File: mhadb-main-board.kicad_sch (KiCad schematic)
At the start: 113 parts, among them J1 Conn_01x04, J10 Conn_01x04_Pin, J2 Conn_01x04, J3 USB_C_Receptacle_USB2.0_14P, J4 Conn_01x02, J5 Conn_01x03, J6 Conn_01x03, J7 Conn_01x04, J8 Conn_01x04, J9 Conn_01x04_Pin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

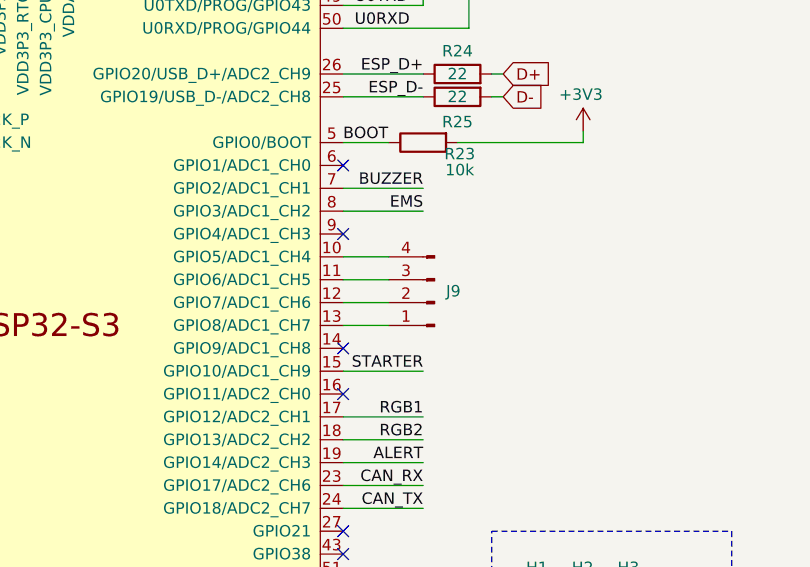
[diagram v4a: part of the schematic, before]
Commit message: pcb: changed outline to 50x50mm
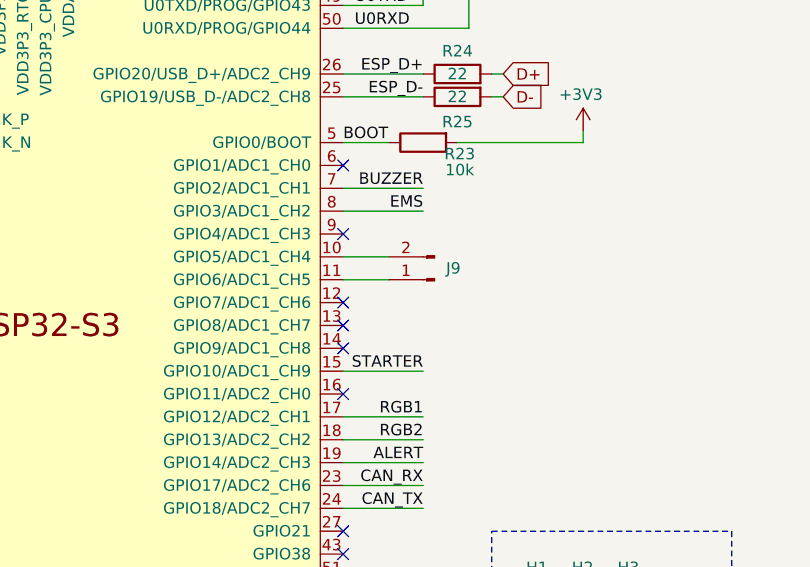
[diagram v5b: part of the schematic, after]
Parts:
- removed J9: Conn_01x04_Pin, Connector_PinHeader_2.54mm:PinHeader_1x04_P2.54mm_Vertical, symbol Connector:Conn_01x04_Pin
- added J9: Conn_01x02_Pin, Connector_PinHeader_2.54mm:PinHeader_1x02_P2.54mm_Vertical, symbol Connector:Conn_01x02_Pin
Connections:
- net at U5.10 (GPIO5/ADC1_CH4): now also J9.2 (Pin_2)
- net at U5.11 (GPIO6/ADC1_CH5): now also J9.1 (Pin_1)
- no-connect marks 28 -> 30
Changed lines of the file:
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@@
 	)
 	(no_connect
+		(at 240.03 90.17)
+	)
+	(no_connect
 		(at 240.03 72.39)
 	)
@@
 		(at 173.99 100.33)
 	)
+	(no_connect
+		(at 240.03 87.63)
+	)
 	(wire
 		(pts
@@
 	(wire
 		(pts
-			(xy 240.03 90.17) (xy 245.11 90.17)
-		)
-		(stroke
-			(width 0)
-			(type default)
-		)
-	)
-	(wire
-		(pts
 			(xy 148.59 92.71) (xy 157.48 92.71)
 		)
@@
 	(wire
 		(pts
-			(xy 240.03 87.63) (xy 245.11 87.63)
-		)
-		(stroke
-			(width 0)
-			(type default)
-		)
-	)
-	(wire
-		(pts
 			(xy 50.8 59.69) (xy 50.8 58.42)
 		)
@@
 		(exclude_from_sim no)
 		(in_bom yes)
-		(on_board yes)
+		(on_board no)
 		(dnp no)
 		(property "Reference" "D15"
@@
 	)
 	(symbol
+		(lib_id "Connector:Conn_01x02_Pin")
+		(at 250.19 85.09 180)
+		(unit 1)
+		(exclude_from_sim no)
+		(in_bom yes)
+		(on_board yes)
+		(dnp no)
+		(fields_autoplaced yes)
+		(property "Reference" "J9"
+			(at 251.46 83.8199 0)
+			(effects
+				(font
+					(size 1.27 1.27)
+				)
+				(justify right)
+			)
+		)
+		(property "Value" "Conn_01x02_Pin"
+			(at 249.555 87.63 0)
+			(effects
+				(font
+					(size 1.27 1.27)
+				)
+				(hide yes)
+			)
+		)
+		(property "Footprint" "Connector_PinHeader_2.54mm:PinHeader_1x02_P2.54mm_Vertical"
+			(at 250.19 85.09 0)
+			(effects
+				(font
+					(size 1.27 1.27)
+				)
+				(hide yes)
+			)
+		)
+		(property "Datasheet" "~"
+			(at 250.19 85.09 0)
+			(effects
+				(font
+					(size 1.27 1.27)
+				)
+				(hide yes)
+			)
+		)
+		(property "Description" "Generic connector, single row, 01x02, script generated"
+			(at 250.19 85.09 0)
+			(effects
+				(font
+					(size 1.27 1.27)
+				)
+				(hide yes)
+			)
+		)
+		(pin "2"
+		)
+		(pin "1"
+		)
+		(instances
+			(project ""
+				(path "/108bdc05-5362-4b20-8d3b-92cc456652bf"
+					(reference "J9")
+					(unit 1)
+				)
+			)
+		)
+	)
+	(symbol
 		(lib_id "power:+5V")
 		(at 81.28 138.43 0)
@@
 		(exclude_from_sim no)
 		(in_bom yes)
-		(on_board yes)
+		(on_board no)
 		(dnp no)
 		(property "Reference" "D14"
@@
 					(unit 1)
 				)
-			)
-		)
-	)
-	(symbol
-		(lib_id "Connector:Conn_01x04_Pin")
-		(at 250.19 87.63 180)
-		(unit 1)
-		(exclude_from_sim no)
-		(in_bom no)
-		(on_board yes)
-		(dnp no)
-		(fields_autoplaced yes)
-		(property "Reference" "J9"
-			(at 251.46 86.3599 0)
-			(effects
-				(font
-					(size 1.27 1.27)
-				)
-				(justify right)
-			)
-		)
-		(property "Value" "Conn_01x04_Pin"
-			(at 252.73 86.36 90)
-			(effects
-				(font
-					(size 1.27 1.27)
-				)
-				(hide yes)
-			)
-		)
-		(property "Footprint" "Connector_PinHeader_2.54mm:PinHeader_1x04_P2.54mm_Vertical"
-			(at 250.19 87.63 0)
-			(effects
-				(font
-					(size 1.27 1.27)
-				)
-				(hide yes)
-			)
-		)
-		(property "Datasheet" "~"
-			(at 250.19 87.63 0)
-			(effects
-				(font
-					(size 1.27 1.27)
-				)
-				(hide yes)
-			)
-		)
-		(property "Description" "Generic connector, single row, 01x04, script generated"
-			(at 250.19 87.63 0)
-			(effects
-				(font
-					(size 1.27 1.27)
-				)
-				(hide yes)
-			)
-		)
-		(pin "4"
-		)
-		(pin "3"
-		)
-		(pin "2"
-		)
-		(pin "1"
-		)
-		(instances
-			(project "mhadb-main-board"
-				(path "/108bdc05-5362-4b20-8d3b-92cc456652bf"
-					(reference "J9")
-					(unit 1)
-				)

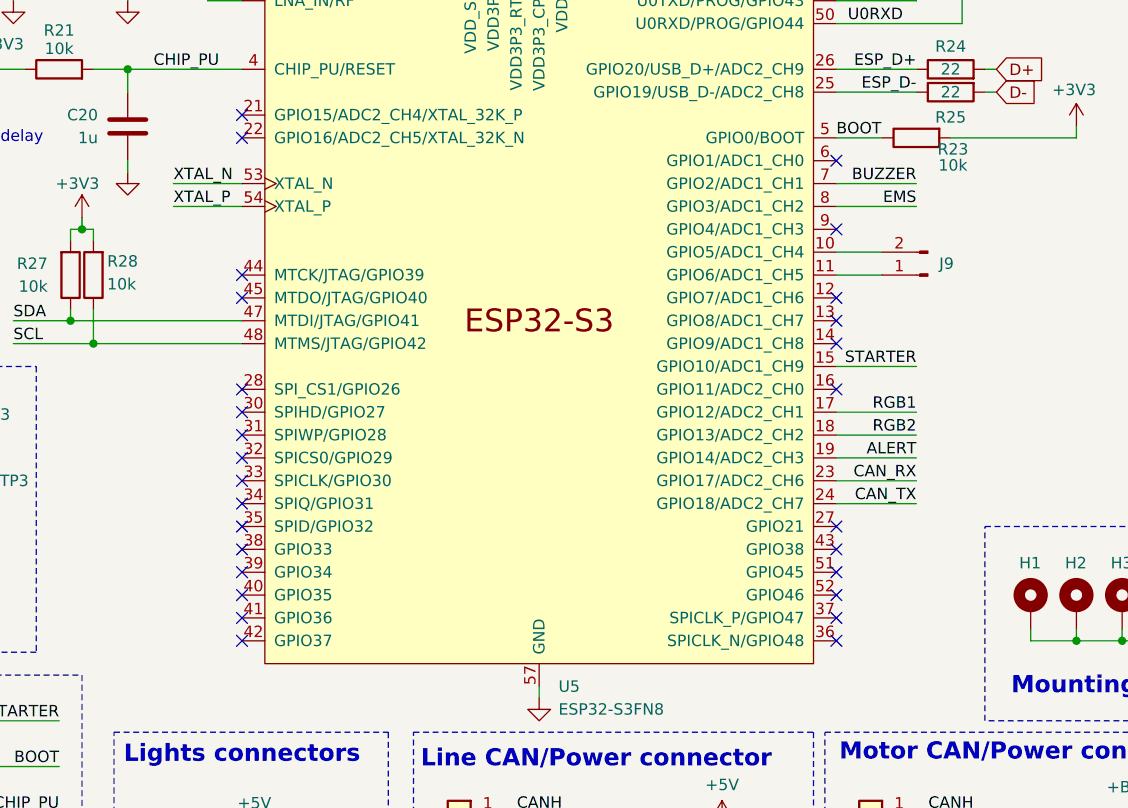
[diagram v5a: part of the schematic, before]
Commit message: schem/pcb: reorganize GPIOs
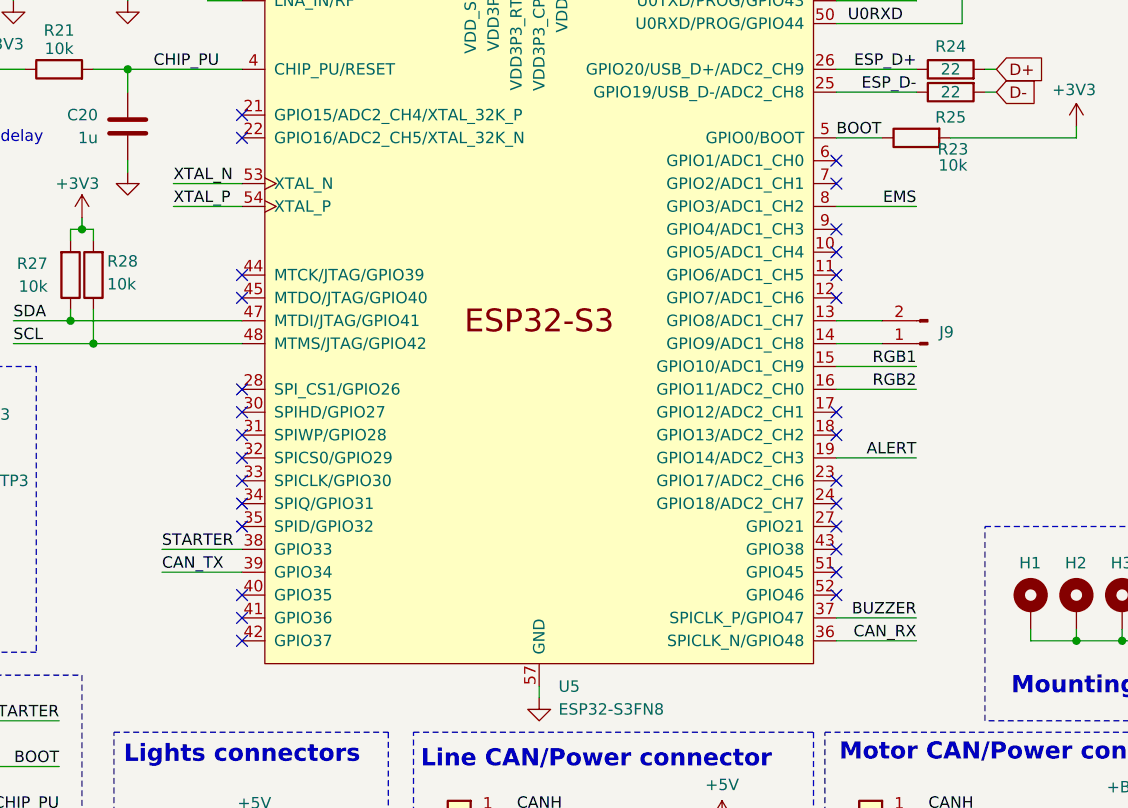
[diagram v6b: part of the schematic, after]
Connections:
- net BUZZER: now also U5.37 (SPICLK_P/GPIO47); no longer U5.7 (GPIO2/ADC1_CH1)
- net CAN_RX: now also U5.36 (SPICLK_N/GPIO48); no longer U5.23 (GPIO17/ADC2_CH6)
- net CAN_TX: now also U5.39 (GPIO34); no longer U5.24 (GPIO18/ADC2_CH7)
- net RGB1: now also U5.15 (GPIO10/ADC1_CH9); no longer U5.17 (GPIO12/ADC2_CH1)
- net RGB2: now also U5.16 (GPIO11/ADC2_CH0); no longer U5.18 (GPIO13/ADC2_CH2)
- net STARTER: now also U5.38 (GPIO33); no longer U5.15 (GPIO10/ADC1_CH9)
- net at J9.1 (Pin_1): now also U5.14 (GPIO9/ADC1_CH8); no longer U5.11 (GPIO6/ADC1_CH5)
- net at J9.2 (Pin_2): now also U5.13 (GPIO8/ADC1_CH7); no longer U5.10 (GPIO5/ADC1_CH4)
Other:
- moved on the sheet: J9

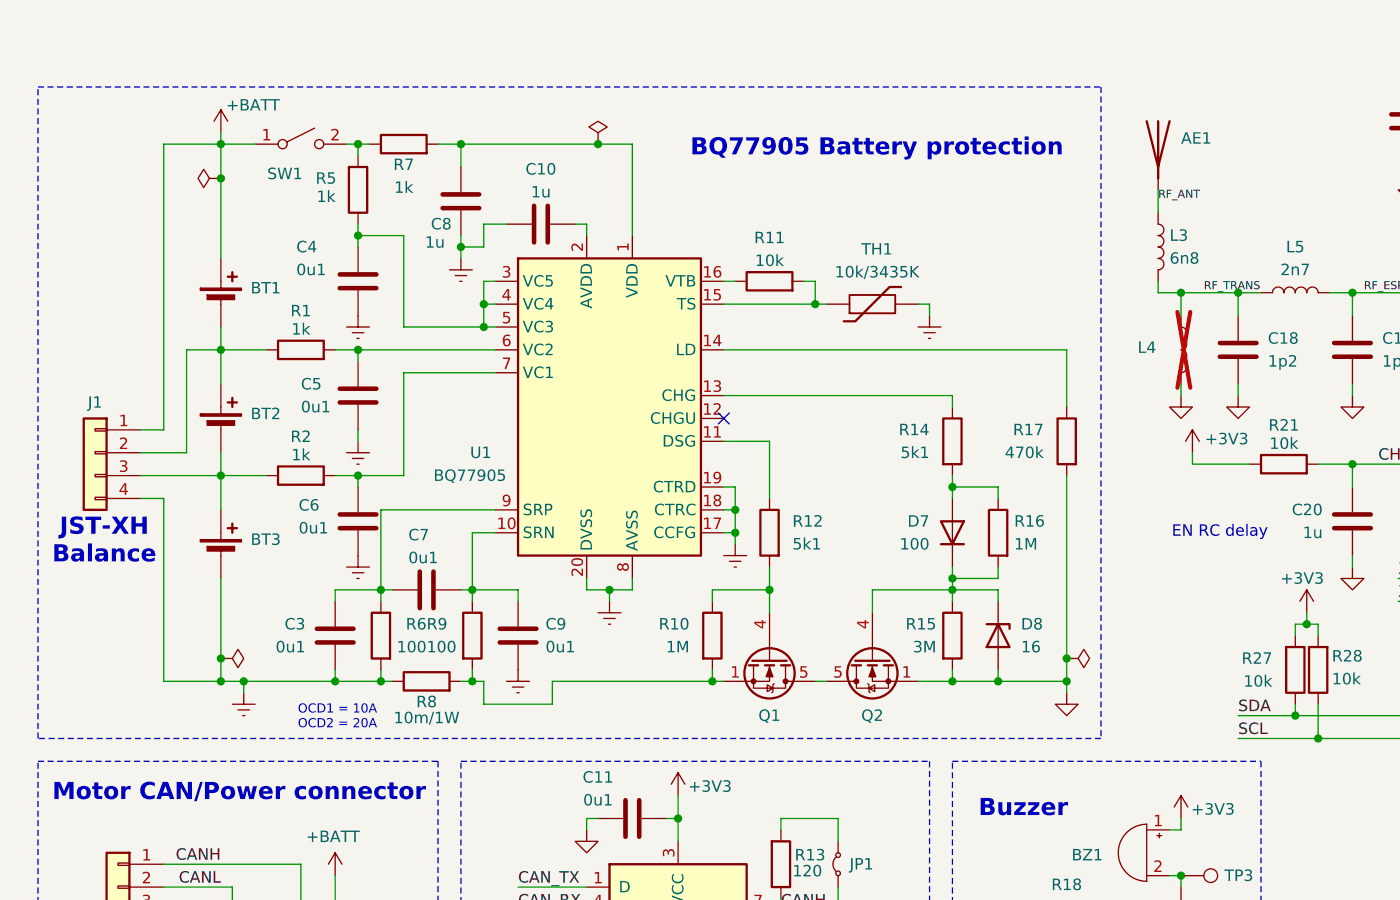
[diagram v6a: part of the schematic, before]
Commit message: pcb: add RF routing
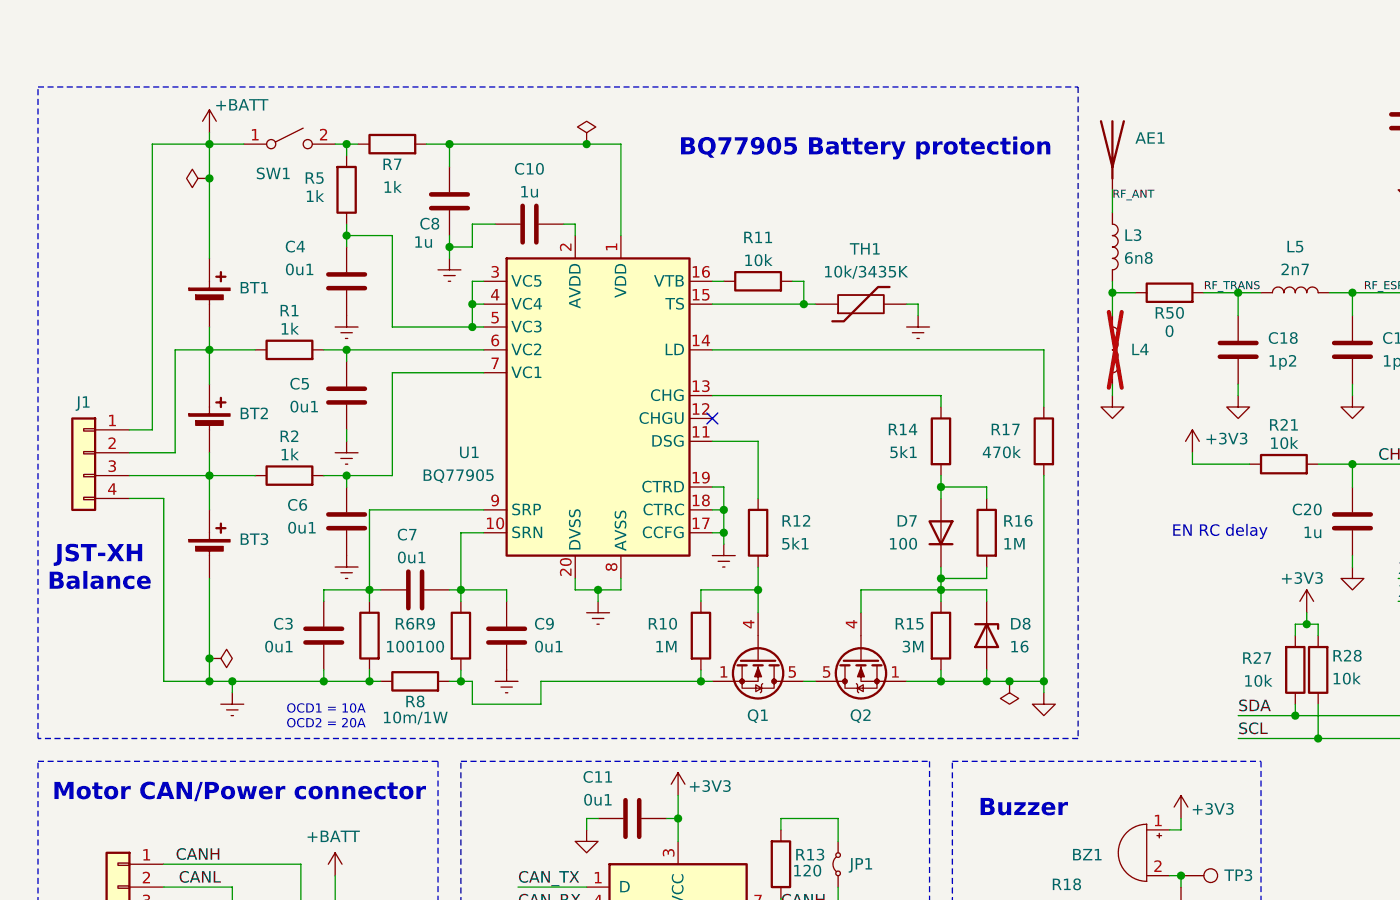
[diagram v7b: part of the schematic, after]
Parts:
- added R50: 0, Resistor_SMD:R_0402_1005Metric, symbol Device:R
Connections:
- net RF_TRANS: now also R50.2; no longer L3.2, L4.1
- new net: L3.2, L4.1, R50.1
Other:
- moved on the sheet: AE1, BT1, BT2, BT3, C10, C3, C4, C5, C6, C7, C8, C9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

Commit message: pcb: add missing connections
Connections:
- net ALERT: now also U5.41 (GPIO36); no longer U5.19 (GPIO14/ADC2_CH3)
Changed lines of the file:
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@@
 	)
 	(no_connect
+		(at 240.03 105.41)
+	)
+	(no_connect
 		(at 173.99 87.63)
 	)
@@
 	)
 	(no_connect
-		(at 173.99 123.19)
+		(at 173.99 120.65)
 	)
 	(no_connect
@@
 	)
 	(no_connect
-		(at 173.99 120.65)
-	)
-	(no_connect
 		(at 173.99 100.33)
 	)
@@
 	(wire
 		(pts
-			(xy 248.92 105.41) (xy 240.03 105.41)
-		)
-		(stroke
-			(width 0)
-			(type default)
-		)
-	)
-	(wire
-		(pts
 			(xy 262.89 41.91) (xy 262.89 43.18)
 		)
@@
 	(wire
 		(pts
+			(xy 165.1 123.19) (xy 173.99 123.19)
+		)
+		(stroke
+			(width 0)
+			(type default)
+		)
+	)
+	(wire
+		(pts
 			(xy 74.93 35.56) (xy 73.66 35.56)
 		)
@@
 		)
 	)
+	(label "ALERT"
+		(at 165.1 123.19 0)
+		(effects
+			(font
+				(size 1.27 1.27)
+			)
+			(justify left bottom)
+		)
+	)
 	(label "ESP_D+"
 		(at 248.92 62.23 180)
@@
 		)
 	)
-	(label "ALERT"
-		(at 248.92 105.41 180)
-		(effects
-			(font
-				(size 1.27 1.27)
-			)
-			(justify right bottom)
-		)
-	)
